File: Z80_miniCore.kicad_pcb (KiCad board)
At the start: 2 copper layers, 31 parts, among them J1 ICSP, J2 UART, J3 I2C, J7 USB_B_Mini, SW1 ON|OFF, SW2 Z80_RESET, U1 Z84C00/PLCC, U2 PIC1-MMU, U3 AS6C4008-55PCN, U4 SST39SF010, Y1 CANNED-DIP8, Y2 Crystal

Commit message: change ROM/footprint -> PLCC32
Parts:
- added C11: 0.1uF, Capacitor_THT:C_Disc_D3.4mm_W2.1mm_P2.50mm, F.Cu at (206.0, 86.8)
- added J5: MicroSD, Connector_PinSocket_2.54mm:PinSocket_1x06_P2.54mm_Vertical, F.Cu at (206.7, 57.8)
- added R10: 10K, Resistor_THT:R_Axial_DIN0207_L6.3mm_D2.5mm_P10.16mm_Horizontal, F.Cu at (206.0, 78.9)
- added R11: 10K, Resistor_THT:R_Axial_DIN0207_L6.3mm_D2.5mm_P10.16mm_Horizontal, F.Cu at (206.0, 82.9)
- added R9: 10K, Resistor_THT:R_Axial_DIN0207_L6.3mm_D2.5mm_P10.16mm_Horizontal, F.Cu at (206.0, 74.8)
- added U5: PIC2-LOADER, Package_DIP:DIP-40_W15.24mm, F.Cu at (187.6, 57.6)
- U4: footprint Package_DIP:DIP-32_W15.24mm -> Package_LCC:PLCC-32_THT-Socket
- moved U4 24.2 mm to (161.2, 77.8)

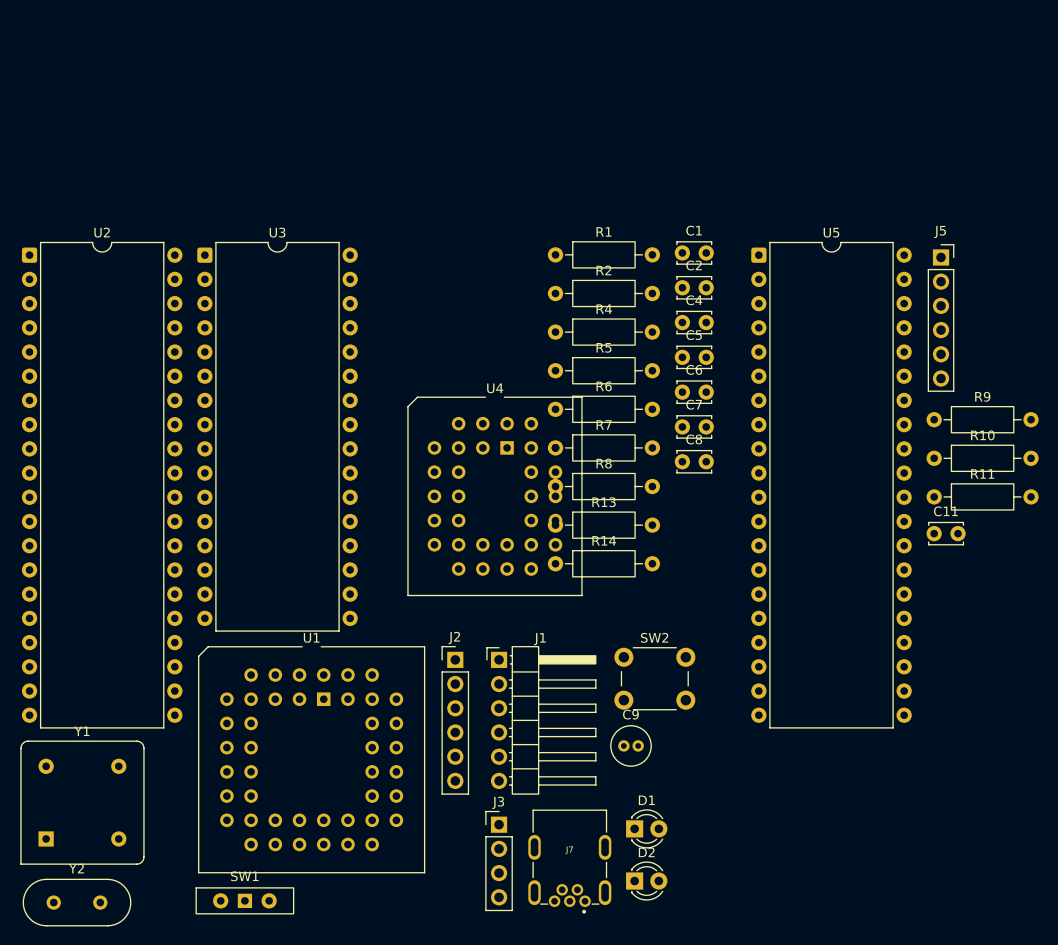
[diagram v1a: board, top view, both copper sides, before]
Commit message: Replace ROM + MMU/74HC138.
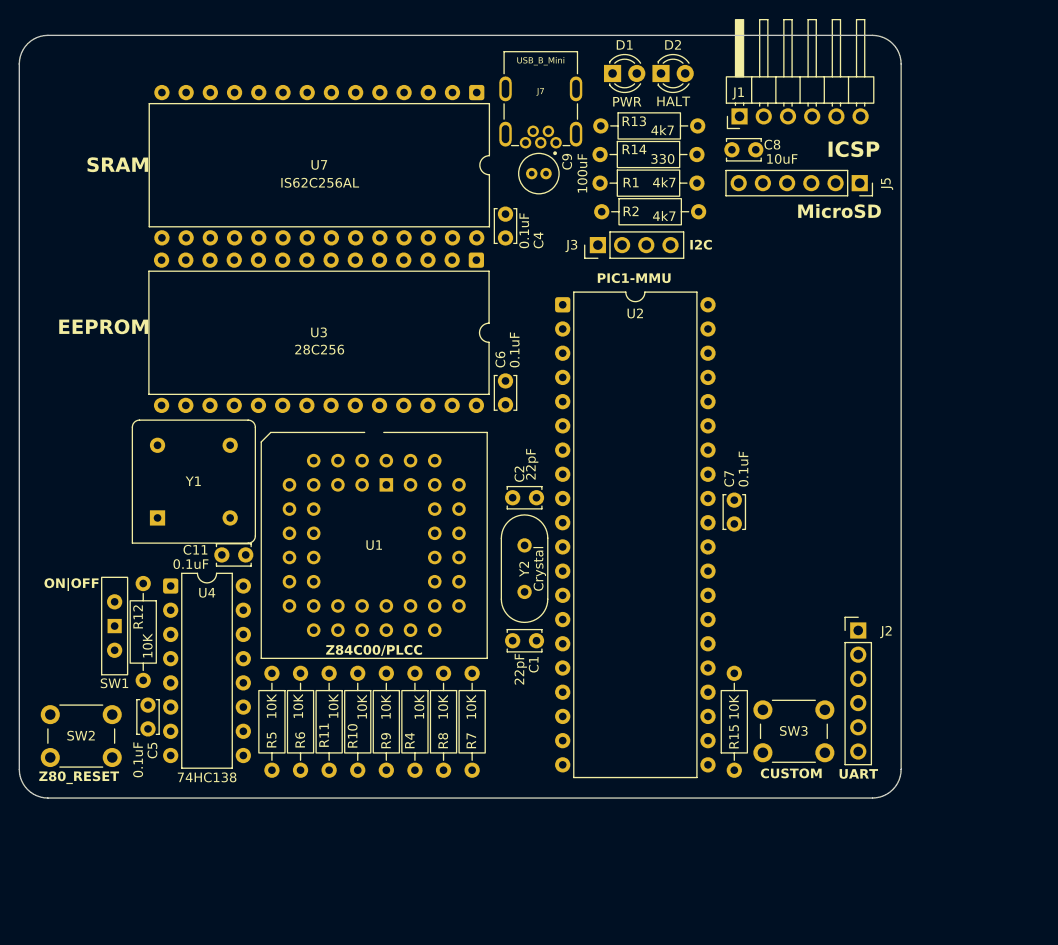
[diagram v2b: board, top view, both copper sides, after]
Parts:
- removed U5: PIC2-LOADER, Package_DIP:DIP-40_W15.24mm
- added R12: 10K, Resistor_THT:R_Axial_DIN0207_L6.3mm_D2.5mm_P10.16mm_Horizontal, F.Cu at (123.0, 92.0)
- added R15: 10K, Resistor_THT:R_Axial_DIN0207_L6.3mm_D2.5mm_P10.16mm_Horizontal, F.Cu at (185.0, 111.6)
- added SW3: CUSTOM, Button_Switch_THT:SW_PUSH_6mm, F.Cu at (188.0, 105.2)
- added U7: IS62C256AL, Package_DIP:DIP-28_W15.24mm, F.Cu at (158.0, 40.5)
- U3: value AS6C4008-55PCN -> 28C256; footprint Package_DIP:DIP-32_W15.24mm -> Package_DIP:DIP-28_W15.24mm
- U4: value SST39SF010 -> 74HC138; footprint Package_LCC:PLCC-32_THT-Socket -> Package_DIP:DIP-16_W7.62mm
- moved D2 84.8 mm to (177.3, 38.5)
- moved J7 79.6 mm to (164.7, 44.9)
- moved D1 79.3 mm to (172.2, 38.5)
- moved C11 74.7 mm to (131.2, 89.0)
- moved C5 68.3 mm to (123.5, 107.2), turned to 90 degrees
- moved R11 66.1 mm to (142.5, 101.4), turned to -90 degrees
- moved R10 64.5 mm to (145.5, 101.4), turned to -90 degrees
- moved R9 63.3 mm to (148.5, 101.4), turned to -90 degrees
- moved J1 62.3 mm to (185.6, 43.0), turned to 90 degrees
- moved Y2 62.0 mm to (163.0, 88.0), turned to -90 degrees
- moved J3 61.7 mm to (170.7, 56.5), turned to 90 degrees
- moved C9 60.8 mm to (163.8, 49.0)
- moved SW2 60.5 mm to (113.2, 105.8)
- moved U2 56.2 mm to (167.0, 62.8)
- moved R5 43.5 mm to (136.5, 101.4), turned to -90 degrees
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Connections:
- U1 pad 5: /A15 -> /Z80_A15
- U2 pad 10: /SRAM_CE -> /A3
- U2 pad 2: /A0 -> /BUTTON
- U2 pad 3: /A1 -> /CS
- U2 pad 4: /A2 -> /SCK
- U2 pad 5: /A3 -> /MOSI
- U2 pad 6: /A16 -> /MISO
- U2 pad 7: /A17 -> /A0
- U2 pad 8: /A18 -> /A1
- U2 pad 9: /ROM_CE -> /A2
- U3 pad 1: /A18 -> /A14
- U3 pad 10: /A2 -> /A0
- U3 pad 11: /A1 -> /D0
- U3 pad 12: /A0 -> /D1
- U3 pad 13: /D0 -> /D2
- U3 pad 14: /D1 -> GND
- U3 pad 15: /D2 -> /D3
- U3 pad 16: GND -> /D4
- U3 pad 17: /D3 -> /D5
- U3 pad 18: /D4 -> /D6
- U3 pad 19: /D5 -> /D7
- U3 pad 2: /A16 -> /A12
- U3 pad 20: /D6 -> /ROM_CE
- U3 pad 21: /D7 -> /A10
- U3 pad 22: /SRAM_CE -> /RD
- U3 pad 23: /A10 -> /A11
- U3 pad 24: /RD -> /A9
- U3 pad 25: /A11 -> /A8
- U3 pad 26: /A9 -> /A13
- U3 pad 27: /A8 -> /WR
- U3 pad 28: /A13 -> VCC
- U3 pad 3: /A14 -> /A7
- U3 pad 4: /A12 -> /A6
- U3 pad 5: /A7 -> /A5
- U3 pad 6: /A6 -> /A4
- U3 pad 7: /A5 -> /A3
- U3 pad 8: /A4 -> /A2
- U3 pad 9: /A3 -> /A1
- U4 pad 1: unconnected-(U4-NC-Pad1) -> /Z80_A15
- U4 pad 10: /A2 -> unconnected-(U4-~{Y5}-Pad10)
- U4 pad 11: /A1 -> unconnected-(U4-~{Y4}-Pad11)
- U4 pad 12: /A0 -> unconnected-(U4-~{Y3}-Pad12)
- U4 pad 13: /D0 -> unconnected-(U4-~{Y2}-Pad13)
- U4 pad 14: /D1 -> /SRAM_CE
- U4 pad 15: /D2 -> /ROM_CE
- U4 pad 16: GND -> VCC
- U4 pad 2: /A16 -> GND
- U4 pad 3: /A15 -> GND
- U4 pad 4: /A12 -> /MREQ
- U4 pad 5: /A7 -> /RFSH
- U4 pad 6: /A6 -> VCC
- U4 pad 7: /A5 -> unconnected-(U4-~{Y7}-Pad7)
- U4 pad 8: /A4 -> GND
- U4 pad 9: /A3 -> unconnected-(U4-~{Y6}-Pad9)
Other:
- board outline added: 92.5 x 80 mm
- board text added: "EEPROM"
- board text added: "SRAM"
